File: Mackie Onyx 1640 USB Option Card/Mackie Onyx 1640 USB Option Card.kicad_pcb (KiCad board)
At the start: 2 copper layers, 2 parts, among them J1 Conn_02x17_Odd_Even, U1 XU316-1024-QF60B-C24

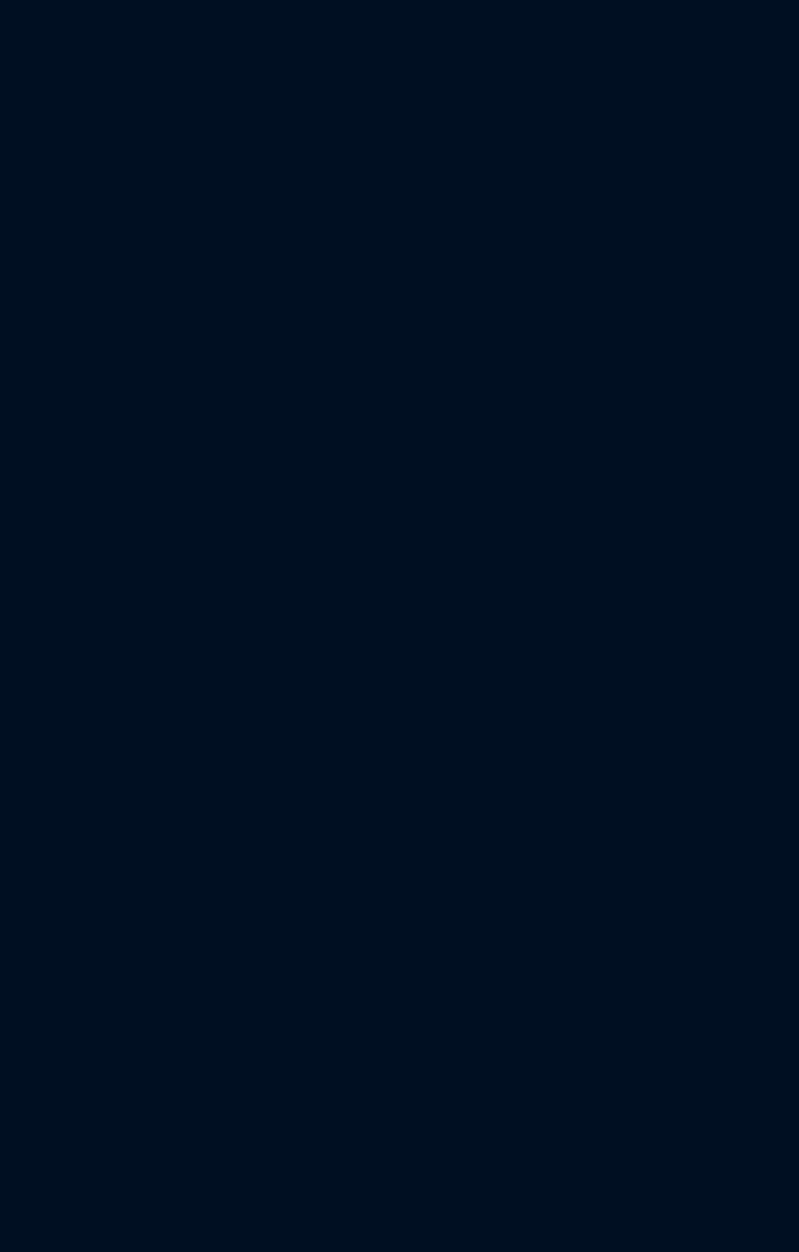
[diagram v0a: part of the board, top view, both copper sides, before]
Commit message: PCB connector documentation added
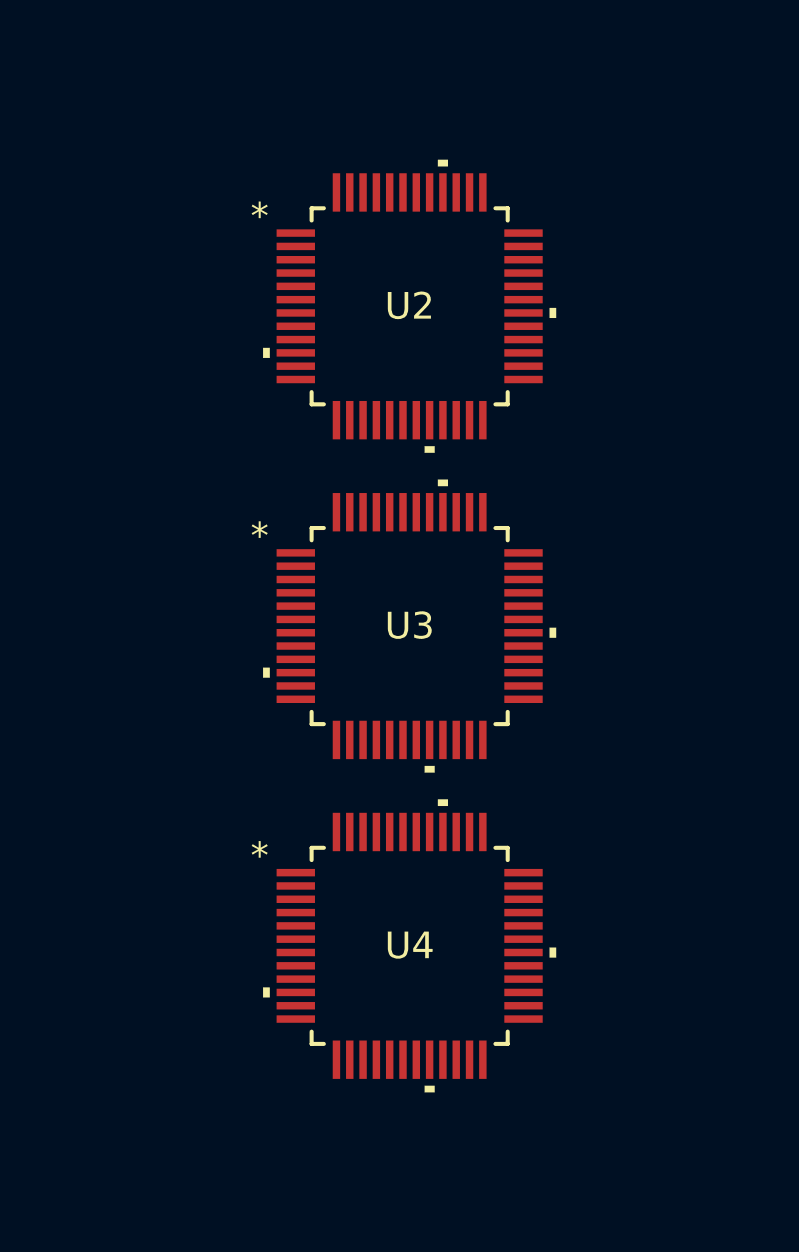
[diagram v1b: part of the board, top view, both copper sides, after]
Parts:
- added U2: CS5368-CQZ, adc:CIR-LQFP-48, F.Cu at (176.2, 48.2)
- added U3: CS5368-CQZ, adc:CIR-LQFP-48, F.Cu at (176.2, 60.3)
- added U4: CS5368-CQZ, adc:CIR-LQFP-48, F.Cu at (176.2, 72.3)
